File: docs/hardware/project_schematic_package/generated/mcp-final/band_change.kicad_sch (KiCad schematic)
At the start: 2 parts, among them U2 74HC4514, U3 ULN2803A

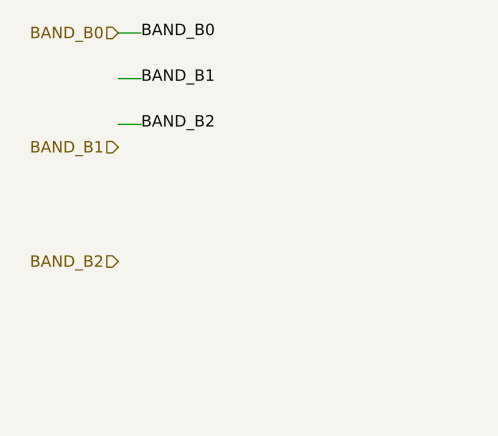
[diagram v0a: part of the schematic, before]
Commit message: Eliminate hierarchy and connector text overlaps
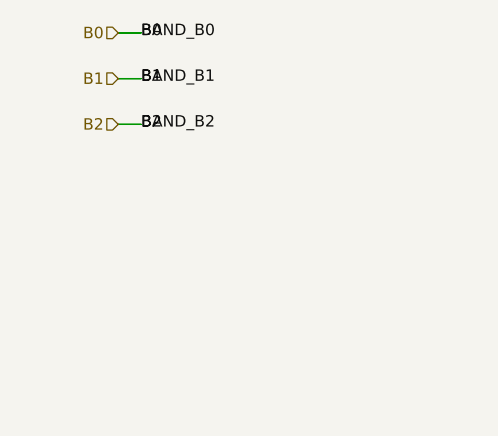
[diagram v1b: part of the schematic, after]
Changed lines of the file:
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@@
 	(generator_version "9.0")
 	(paper "A4")
-	(hierarchical_label "BAND_B0"
-	(shape input)
-	(at 25.4 25.4 180)
-	(effects
-		(font
-			(size 1.27 1.27)
-		)
-	)
-)
-	(hierarchical_label "BAND_B1"
-	(shape input)
-	(at 25.4 38.1 180)
-	(effects
-		(font
-			(size 1.27 1.27)
-		)
-	)
-)
-	(hierarchical_label "BAND_B2"
-	(shape input)
-	(at 25.4 50.8 180)
-	(effects
-		(font
-			(size 1.27 1.27)
-		)
+	(wire
+	(pts
+		(xy 25.4 25.4) (xy 27.94 25.4)
+	)
+	(stroke
+		(width 0)
+		(type default)
+	)
+)
+	(wire
+	(pts
+		(xy 25.4 30.48) (xy 27.94 30.48)
+	)
+	(stroke
+		(width 0)
+		(type default)
+	)
+)
+	(wire
+	(pts
+		(xy 25.4 35.56) (xy 27.94 35.56)
+	)
+	(stroke
+		(width 0)
+		(type default)
 	)
 )
@@
 )
 	(label "BAND_B2"
+	(at 27.94 35.56 0)
+	(effects
+		(font
+			(size 1.27 1.27)
+		)
+	)
+)
+	(label "B0"
+	(at 27.94 25.4 0)
+	(effects
+		(font
+			(size 1.27 1.27)
+		)
+	)
+)
+	(label "B1"
+	(at 27.94 30.48 0)
+	(effects
+		(font
+			(size 1.27 1.27)
+		)
+	)
+)
+	(label "B2"
 	(at 27.94 35.56 0)
 	(effects
@@
 		)
 	)
+)
+	(hierarchical_label "B0"
+	(shape input)
+	(at 25.4 25.4 180)
+	(effects
+		(font
+			(size 1.27 1.27)
+		)
+	)
+)
+	(hierarchical_label "B1"
+	(shape input)
+	(at 25.4 30.48 180)
+	(effects
+		(font
+			(size 1.27 1.27)
+		)
+	)
+)
+	(hierarchical_label "B2"
+	(shape input)
+	(at 25.4 35.56 180)
+	(effects
+		(font
+			(size 1.27 1.27)
+		)
+	)
